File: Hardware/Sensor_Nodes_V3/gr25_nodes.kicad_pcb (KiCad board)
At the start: 4 copper layers, 22.1 x 70 mm, 72 parts, among them J1 Conn_01x06_Socket, J2 Conn_01x27_Socket, J3 Conn_01x27_Socket, Q1 S9013, U1 STM32F103C8Tx, U2 STM32G474RBTx, U3 MCP2542FDxMF, U4 MCP2542FDxMF, U5 AMS1117-3.3, U6 TPS563200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

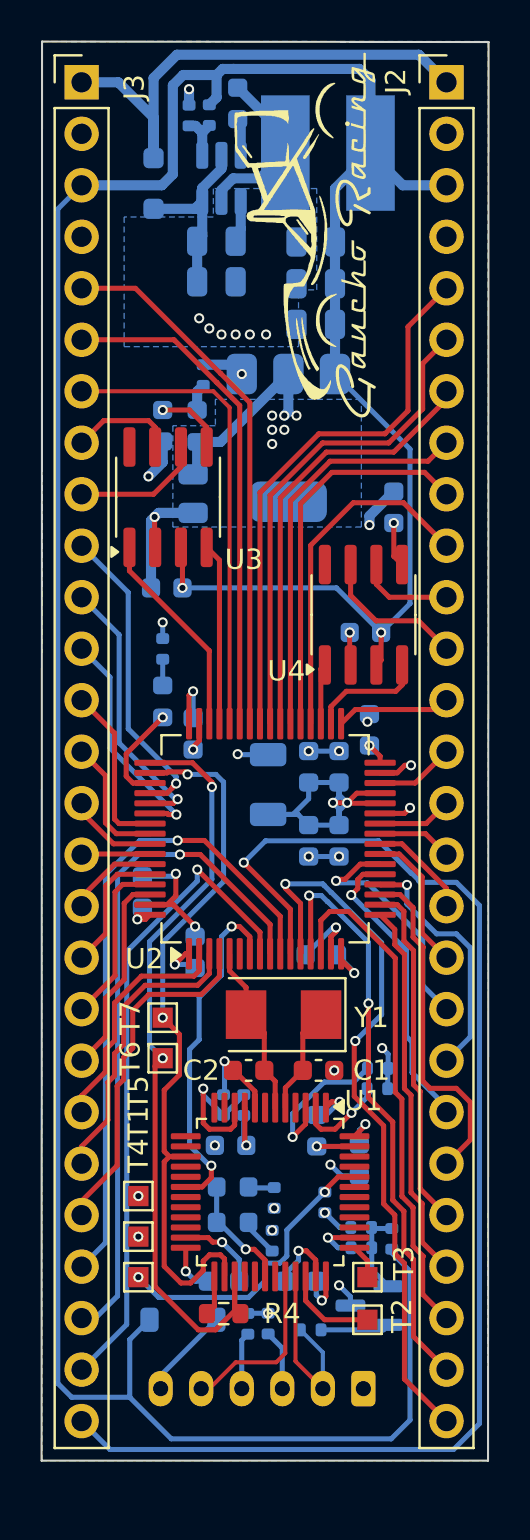
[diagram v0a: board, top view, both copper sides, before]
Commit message: some alt placement finished, moved xtal. will branch and rotate stlink by 90
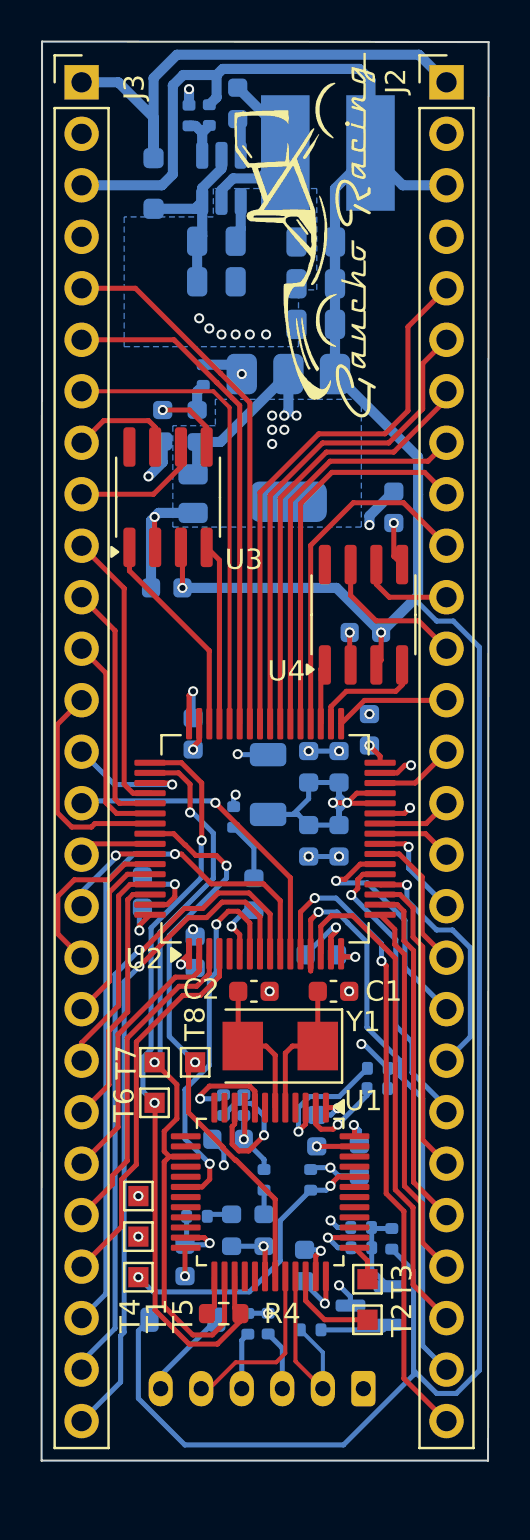
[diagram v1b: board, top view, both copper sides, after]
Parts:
- added T8: ~, TestPoint:TestPoint_Pad_1.0x1.0mm, F.Cu at (116.3, 78.1)
- moved D4 10.5 mm to (119.2, 69.8)
- moved R15 9.00 mm to (118.2, 66.0)
- moved C1 3.97 mm to (123.1, 74.6)
- moved R9 3.92 mm to (116.4, 85.7), turned to 0 degrees
- moved C2 3.91 mm to (119.2, 74.6), turned to 0 degrees
- moved R8 3.03 mm to (119.7, 83.9)
- moved T6 2.24 mm to (114.3, 80.1)
- moved T7 2.24 mm to (114.3, 78.1)
- moved C5 2.16 mm to (115.8, 87.9), turned to 90 degrees
- moved D2 2.14 mm to (118.1, 86.4), turned to -90 degrees
- moved D1 1.60 mm to (119.7, 86.4), turned to 90 degrees
- moved Y1 1.56 mm to (120.5, 77.3)
- moved R1 1.31 mm to (122.0, 83.9), turned to 90 degrees
- moved C3 0.80 mm to (121.7, 88.1), turned to 90 degrees
- moved C4 0.32 mm to (117.9, 81.9)
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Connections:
- J3 pad 14: PB3 -> PA15
- J3 pad 15: PB4 -> PC3
- J3 pad 16: PB5 -> PB4
- J3 pad 17: PB6 -> PB5
- J3 pad 18: I2C1_SDA -> PB6
- J3 pad 19: I2C1_SCL -> I2C1_SDA
- J3 pad 20: PB9 -> I2C1_SCL
- J3 pad 21: PC13 -> PB9
- J3 pad 22: PC14 -> PC13
- J3 pad 23: PC15 -> PC14
- J3 pad 24: PC2 -> PC15
- J3 pad 25: PC1 -> PC2
- J3 pad 26: PC0 -> PC1
- J3 pad 27: PC3 -> PC0
- U1 pad 29: unconnected-(U1-PA8-Pad29) -> MCO
- U1 pad 31: unconnected-(U1-PA10-Pad31) -> T_SWO
- U2 pad 5: XTAL_S -> MCO
- U2 pad 51: HBEAT -> PA15
- U2 pad 56: PB3 -> T_SWO
- U2 pad 6: unconnected-(U2-PF1-Pad6) -> HBEAT
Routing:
- net PC3: track 65.2 -> 15.7 mm
- net T_SWO: track 0.00 -> 28.3 mm, vias 0 -> 2
- net +5V: track 163.6 -> 148.2 mm
- net PB3: track 6.42 -> 0.00 mm
- net PA15: track 0.00 -> 6.26 mm, vias 0 -> 1
- net PB6: track 4.50 -> 8.72 mm
- net PA0: track 35.8 -> 32.2 mm
- net PD2: track 8.38 -> 11.0 mm
- net LED: track 5.71 -> 3.12 mm
- net T_CLK: track 35.8 -> 38.3 mm
- net PB9: track 10.1 -> 12.6 mm
- net I2C1_SCL: track 8.34 -> 10.7 mm
- net I2C1_SDA: track 6.46 -> 8.71 mm
- net PC2: track 32.5 -> 34.8 mm
- net GND: track 57.9 -> 55.9 mm
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- added copper zone on In1.Cu, net +3.3V
- added copper zone on In1.Cu, net CANH2
- added copper zone on In2.Cu, net GND
- removed copper zone on B.Cu, net (none)
- removed copper zone on F.Cu, net (none)
- removed copper zone on In2.Cu, net +3.3V
- removed copper zone on In1.Cu, net GND

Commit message: fixed placement, added some decals, now using clock from stlink
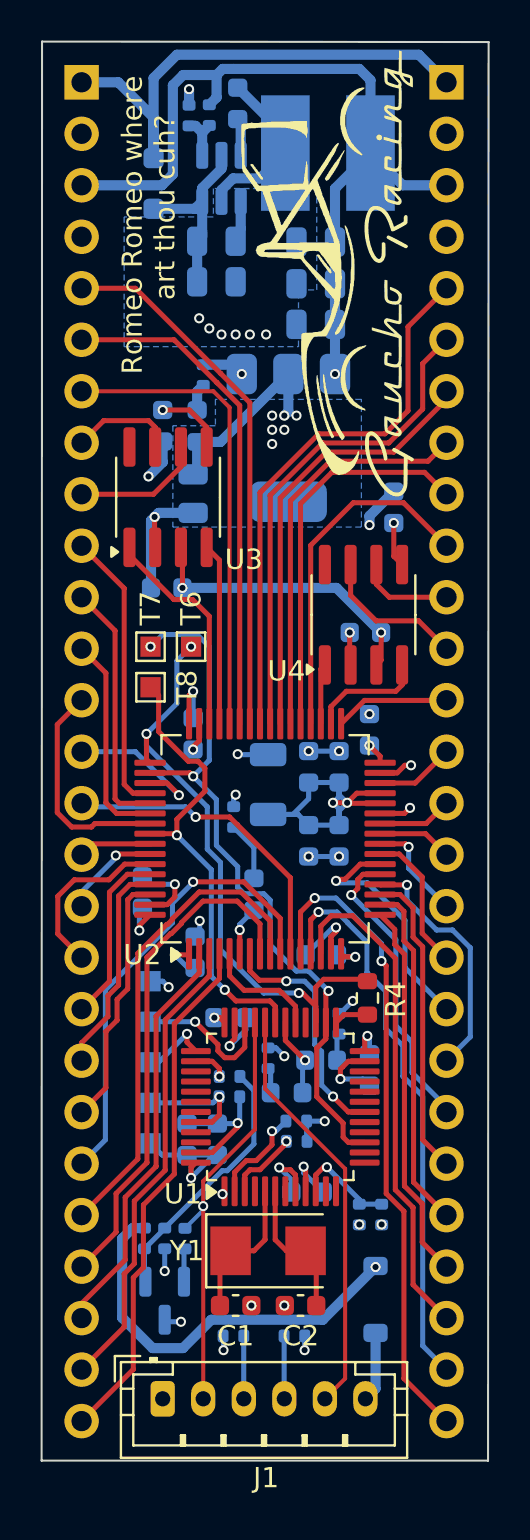
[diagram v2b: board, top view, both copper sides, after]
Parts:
- J1: moved to F.Cu
- J2, J3, T1, T2, T3, T4, T5: moved to B.Cu
- L2: footprint Inductor_SMD:L_Cenker_CKCS6045 -> Inductor_SMD:L_Cenker_CKCS6020
- moved T6 22.6 mm to (116.1, 57.6)
- moved T7 20.5 mm to (114.1, 57.6)
- moved T8 18.6 mm to (114.1, 59.6)
- moved T2 18.2 mm to (114.1, 76.1), turned to 180 degrees
- moved R4 17.1 mm to (124.8, 74.9), turned to 90 degrees
- moved C1 16.2 mm to (118.3, 90.1)
- moved C2 15.7 mm to (121.5, 90.1), turned to 180 degrees
- moved T3 15.1 mm to (114.1, 78.1), turned to 180 degrees
- moved R12 12.2 mm to (113.8, 86.8), turned to 90 degrees
- moved R9 11.8 mm to (123.4, 76.2), turned to -90 degrees
- moved R14 10.7 mm to (118.0, 78.8)
- moved T5 10.6 mm to (114.1, 74.1), turned to 180 degrees
- moved C3 10.2 mm to (124.9, 78.5), turned to -90 degrees
- moved Y1 10.1 mm to (119.9, 87.4), turned to 0 degrees
- moved Q1 10.1 mm to (114.8, 89.9), turned to -90 degrees
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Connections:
- J3 pad 22: PC13 -> PC2
- J3 pad 23: PC14 -> PC1
- J3 pad 24: PC15 -> PC0
- J3 pad 25: PC2 -> PC13
- J3 pad 26: PC1 -> PC14
- J3 pad 27: PC0 -> PC15
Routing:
- net +5V: track 148.2 -> 123.4 mm, vias 2 -> 4
- net D-: track 8.66 -> 21.4 mm
- net PC2: track 34.8 -> 23.0 mm
- net D+: track 9.46 -> 21.1 mm, vias 0 -> 1
- net B0: track 14.5 -> 5.70 mm, vias 2 -> 1
- net Net-(Q1-B): track 4.27 -> 12.8 mm
- net PC1: track 31.9 -> 24.1 mm, vias 1 -> 0
- net T_DIO: track 38.1 -> 30.3 mm, vias 2 -> 3
- net PC0: track 33.0 -> 25.3 mm, vias 1 -> 0
- net PC14: track 16.0 -> 23.1 mm
- net PC15: track 18.8 -> 25.9 mm
- net PC13: track 13.3 -> 20.4 mm
- net T_RST: track 18.8 -> 11.9 mm
- net MCO: track 0.00 -> 5.76 mm
- net T_SWO: track 28.3 -> 22.8 mm
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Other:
- board text added: "@an0tv 10/2/24"
- board text added: "Romeo Romeo where art thou cuh?"

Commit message: flipped GND and 3v3 layer
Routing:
- added copper zone on In2.Cu, net +3.3V
- added copper zone on In1.Cu, net GND
- removed copper zone on In1.Cu, net +3.3V
- removed copper zone on In1.Cu, net CANH2
- removed copper zone on In2.Cu, net GND
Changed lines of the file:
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@@
 		(tags "resistor")
 		(property "Reference" "R10"
-			(at 0.690001 1.9 90)
+			(at -0.009999 1.1 180)
 			(layer "B.SilkS")
 			(effects
@@
 		(tags "resistor")
 		(property "Reference" "R7"
-			(at 2.1 -5.1 90)
+			(at 0 -1.1 180)
 			(layer "B.SilkS")
 			(effects
@@
 	)
 	(segment
-		(start 119.313604 82.95)
-		(end 118.82084 82.95)
+		(start 118.82084 82.95)
+		(end 118.25 83.52084)
 		(width 0.25)
 		(layer "F.Cu")
@@
 	)
 	(segment
-		(start 118.82084 82.95)
-		(end 118.25 83.52084)
+		(start 120 81)
+		(end 120 82.263604)
 		(width 0.25)
 		(layer "F.Cu")
@@
 	)
 	(segment
-		(start 120.091797 82.171807)
+		(start 120 82.263604)
 		(end 119.313604 82.95)
 		(width 0.25)
@@
 	)
 	(segment
-		(start 120.091797 81.49807)
-		(end 120.091797 82.171807)
+		(start 118.25 83.52084)
+		(end 118.25 84.4625)
 		(width 0.25)
 		(layer "F.Cu")
@@
 	)
 	(segment
-		(start 118.25 83.52084)
-		(end 118.25 84.4625)
+		(start 119.313604 82.95)
+		(end 118.82084 82.95)
 		(width 0.25)
 		(layer "F.Cu")
@@
 	)
 	(via
-		(at 120.091797 81.49807)
+		(at 120 81)
 		(size 0.5)
 		(drill 0.3)
@@
 	)
 	(segment
-		(start 120.091797 81.49807)
-		(end 120.281932 81.49807)
-		(width 0.25)
-		(layer "B.Cu")
-		(net 82)
-	)
-	(segment
-		(start 120.281932 81.49807)
+		(start 120 81)
 		(end 120.780002 81)
 		(width 0.25)
@@
 	)
 	(zone
-		(net 46)
-		(net_name "CANH2")
+		(net 1)
+		(net_name "GND")
 		(layer "In1.Cu")
 		(hatch edge 0.5)
@@
 		(net 4)
 		(net_name "+3.3V")
-		(layer "In1.Cu")
+		(layer "In2.Cu")
 		(hatch edge 0.5)
-		(priority 1)
+		(priority 2)
 		(connect_pads
 			(clearance 0.5)
@@
 			(thermal_gap 0.5)
 			(thermal_bridge_width 0.5)
+			(island_removal_mode 1)
+			(island_area_min 10)
 		)
 		(polygon
@@
 	)
 	(zone
-		(net 1)
-		(net_name "GND")
+		(net 4)
+		(net_name "+3.3V")
 		(layer "In2.Cu")
 		(hatch edge 0.5)
-		(priority 2)
+		(priority 1)
 		(connect_pads
 			(clearance 0.5)
@@
 			(thermal_gap 0.5)
 			(thermal_bridge_width 0.5)
-			(island_removal_mode 1)
-			(island_area_min 10)
 		)
 		(polygon
